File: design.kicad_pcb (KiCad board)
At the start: 2 copper layers, 54.1 x 73.1 mm, 64 parts, among them J2 Programming, J3 HRO_TYPE-C-31-M-12, Q1 Q_PMOS_GSD, SW1 Control, SW2 EN, SW3 IO0, U1 MCP1700-3302E_SOT23, U2 TCK127BG, U3 AP3015, U4 ESP32-C3-WROOM-02-N4, U5 TTP223, U6 TTP223

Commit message: PCB small silkscreen move
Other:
- board text added: "Vbat"
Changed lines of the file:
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@@
     (fp_line (start 9 -3.67) (end 9 -10) (layer "F.SilkS") (width 0.127))
     (fp_line (start 9 -10) (end -9 -10) (layer "F.SilkS") (width 0.127))
-    (fp_circle (center -10.5 -2.9) (end -10.4 -2.9) (layer "F.SilkS") (width 0.2) (fill none))
+    (fp_circle (center -10.22 -2.9) (end -10.12 -2.9) (layer "F.SilkS") (width 0.2) (fill none))
     (fp_line (start 9.75 10.25) (end 9.75 -10.25) (layer "F.CrtYd") (width 0.05))
     (fp_line (start -9.75 10.25) (end 9.75 10.25) (layer "F.CrtYd") (width 0.05))
@@
     (fp_line (start -9 10) (end 9 10) (layer "F.Fab") (width 0.127))
     (fp_line (start 9 10) (end 9 -4) (layer "F.Fab") (width 0.127))
-    (fp_circle (center -10.5 -2.9) (end -10.4 -2.9) (layer "F.Fab") (width 0.2) (fill none))
+    (fp_circle (center -10.22 -2.9) (end -10.12 -2.9) (layer "F.Fab") (width 0.2) (fill none))
     (pad "1" smd rect (at -8.75 -2.9) (size 1.5 0.9) (layers "F.Cu" "F.Paste" "F.Mask")
       (net 2 "+3.3V") (pinfunction "3V3") (pintype "power_in"))
@@
     (effects (font (size 0.5 0.5) (thickness 0.1)))
   )
+  (gr_text "Vbat" (at 166.8 105.5 90) (layer "F.SilkS")
+    (effects (font (size 0.5 0.5) (thickness 0.1)))
+  )

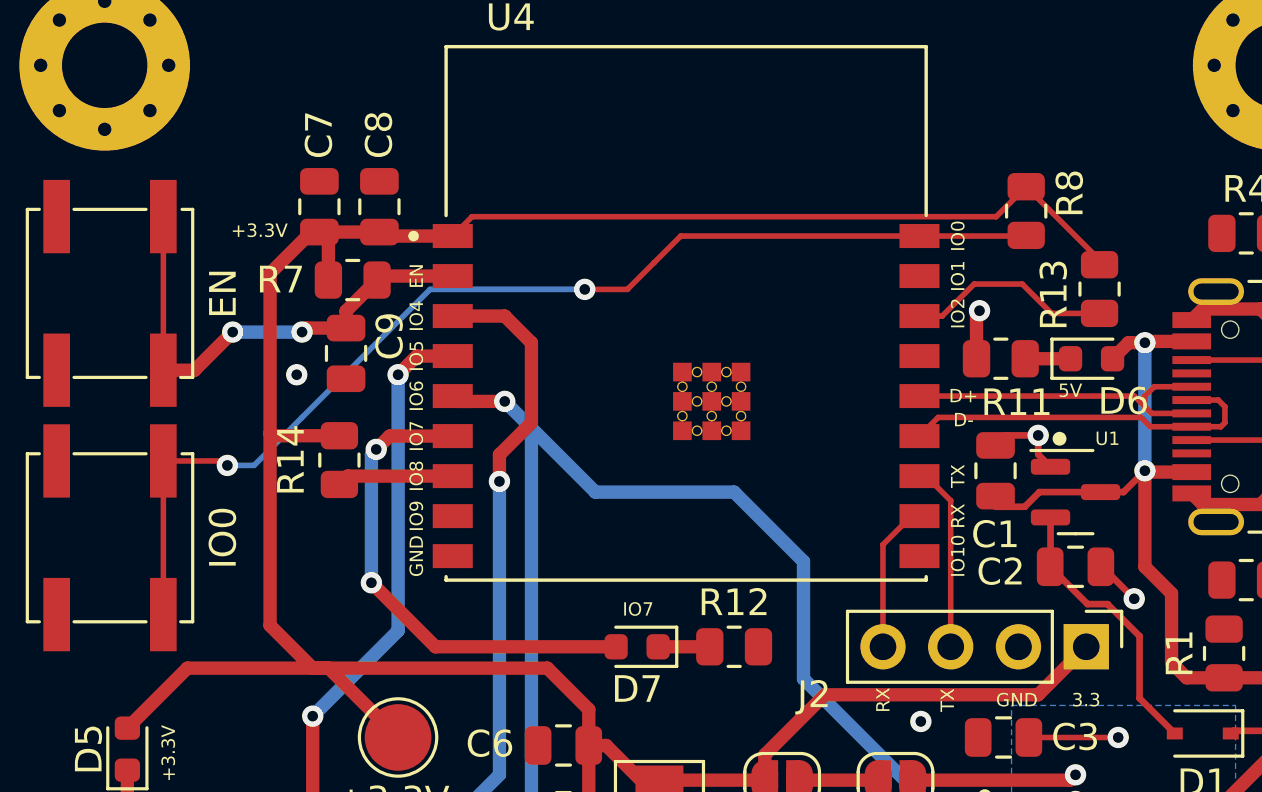
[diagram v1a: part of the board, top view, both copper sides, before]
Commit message: pin IO9 connect to push button instead of IO0 (#11)
* pin IO9 connect to push button instead of IO0
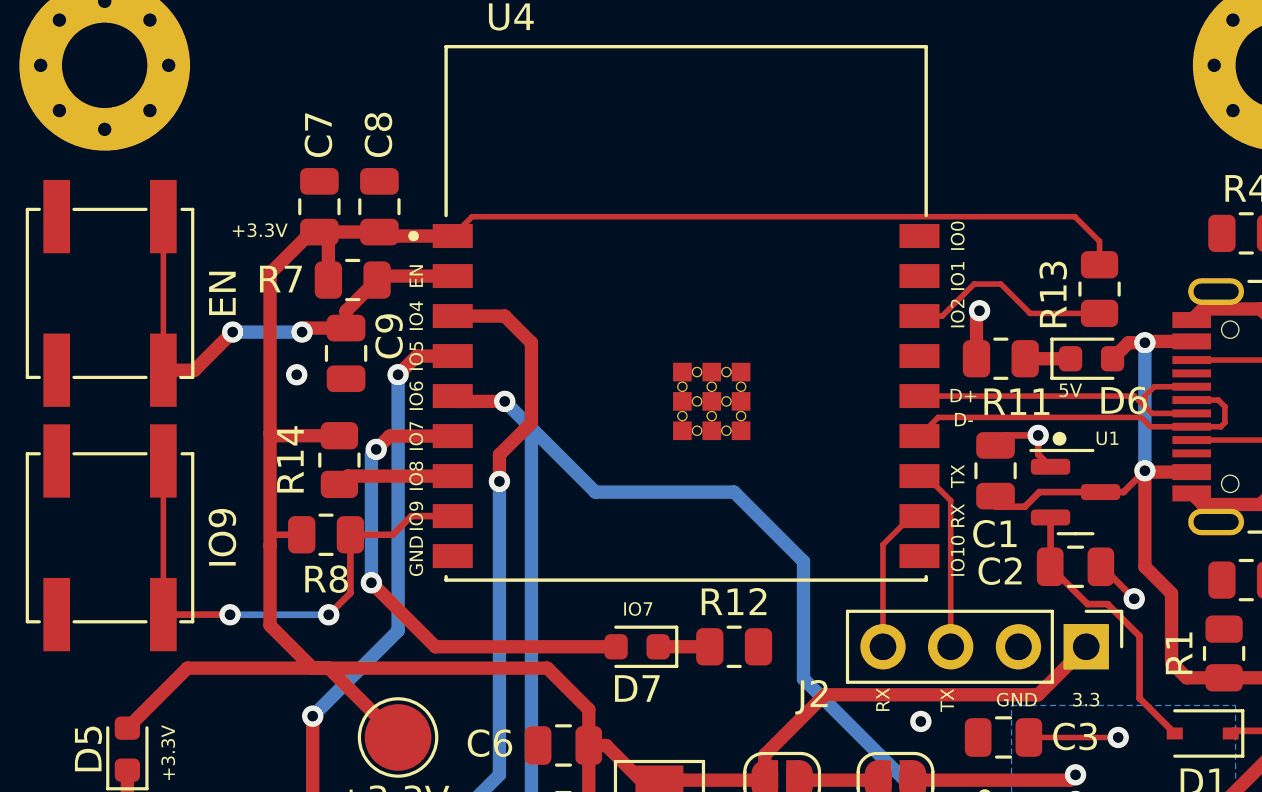
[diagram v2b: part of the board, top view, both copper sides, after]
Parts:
- SW3: value IO0 -> IO9
- moved R8 28.9 mm to (127.5, 87.0), turned to 0 degrees
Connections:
- R8 pad 2: /IO0 -> IO9
- SW3 pad 2: /IO0 -> IO9
- U4 pad 18: /IO0 -> IO0
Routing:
- net /IO0: track 41.8 -> 0.00 mm, vias 2 -> 0
- net IO9: track 0.00 -> 19.4 mm, vias 0 -> 2
- net +3.3V: track 110.7 -> 111.7 mm
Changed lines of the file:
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@@
   (net 32 "/EN")
   (net 33 "/control")
-  (net 34 "/IO0")
+  (net 34 "IO0")
   (net 35 "D+")
   (net 36 "/CC1")
@@
   )
   (footprint "Resistor_SMD:R_0805_2012Metric" (layer "F.Cu")
-    (at 153.75 74.8625 -90)
+    (at 127.5 87)
     (descr "Resistor SMD 0805 (2012 Metric), square (rectangular) end terminal, IPC_7351 nominal, (Body size source: IPC-SM-782 page 72, https://www.pcb-3d.com/wordpress/wp-content/uploads/ipc-sm-782a_amendment_1_and_2.pdf), generated with kicad-footprint-generator")
     (tags "resistor")
@@
     (property "Sheetname" "")
     (attr smd)
-    (fp_text reference "R8" (at -0.6625 -1.65 90) (layer "F.SilkS")
+    (fp_text reference "R8" (at 0 1.7) (layer "F.SilkS")
       (effects (font (size 1 1) (thickness 0.15)))
     )
-    (fp_text value "10K" (at 0 1.65 90) (layer "F.Fab")
+    (fp_text value "10K" (at 0 1.65) (layer "F.Fab")
       (effects (font (size 1 1) (thickness 0.15)))
     )
-    (fp_text user "${REFERENCE}" (at 0 0 90) (layer "F.Fab")
+    (fp_text user "${REFERENCE}" (at 0 0) (layer "F.Fab")
       (effects (font (size 0.5 0.5) (thickness 0.08)))
     )
@@
     (fp_line (start 1 0.625) (end -1 0.625) (layer "F.Fab") (width 0.1))
     (fp_line (start -1 0.625) (end -1 -0.625) (layer "F.Fab") (width 0.1))
-    (pad "1" smd roundrect (at -0.9125 0 270) (size 1.025 1.4) (layers "F.Cu" "F.Paste" "F.Mask") (roundrect_rratio 0.243902)
+    (pad "1" smd roundrect (at -0.9125 0) (size 1.025 1.4) (layers "F.Cu" "F.Paste" "F.Mask") (roundrect_rratio 0.243902)
       (net 2 "+3.3V") (pintype "passive"))
-    (pad "2" smd roundrect (at 0.9125 0 270) (size 1.025 1.4) (layers "F.Cu" "F.Paste" "F.Mask") (roundrect_rratio 0.243902)
-      (net 34 "/IO0") (pintype "passive"))
+    (pad "2" smd roundrect (at 0.9125 0) (size 1.025 1.4) (layers "F.Cu" "F.Paste" "F.Mask") (roundrect_rratio 0.243902)
+      (net 15 "IO9") (pintype "passive"))
     (model "${KICAD6_3DMODEL_DIR}/Resistor_SMD.3dshapes/R_0805_2012Metric.wrl"
       (offset (xyz 0 0 0))
@@
       (effects (font (size 1 1) (thickness 0.15)))
     )
-    (fp_text value "IO0" (at 0 4.25 90) (layer "F.SilkS")
+    (fp_text value "IO9" (at 0 4.25 90) (layer "F.SilkS")
       (effects (font (size 1 1) (thickness 0.15)))
     )
@@
       (net 1 "GND") (pinfunction "1") (pintype "passive"))
     (pad "2" smd rect (at 2.88 2 90) (size 2.75 1) (layers "F.Cu" "F.Paste" "F.Mask")
-      (net 34 "/IO0") (pinfunction "2") (pintype "passive"))
+      (net 15 "IO9") (pinfunction "2") (pintype "passive"))
     (pad "2" smd rect (at -2.88 2 90) (size 2.75 1) (layers "F.Cu" "F.Paste" "F.Mask")
-      (net 34 "/IO0") (pinfunction "2") (pintype "passive"))
+      (net 15 "IO9") (pinfunction "2") (pintype "passive"))
     (model "${KICAD6_3DMODEL_DIR}/Button_Switch_SMD.3dshapes/SW_SPST_EVPBF.wrl"
       (offset (xyz 0 0 0))
@@
       (net 11 "IO1") (pinfunction "IO1") (pintype "bidirectional"))
     (pad "18" smd rect (at 8.75 -2.9) (size 1.5 0.9) (layers "F.Cu" "F.Paste" "F.Mask")
-      (net 34 "/IO0") (pinfunction "IO0") (pintype "bidirectional"))
+      (net 34 "IO0") (pinfunction "IO0") (pintype "bidirectional"))
     (pad "19" smd rect (at -0.14 2.2) (size 0.7 0.7) (layers "F.Cu" "F.Paste" "F.Mask")
       (net 1 "GND") (pinfunction "GND") (pintype "power_in"))
@@
   (segment (start 126.95 75.65) (end 127.25 75.65) (width 0.5) (layer "F.Cu") (net 2))
   (segment (start 129.5 75.65) (end 127.25 75.65) (width 0.5) (layer "F.Cu") (net 2))
-  (segment (start 153.75 73.95) (end 152.625 75.075) (width 0.21) (layer "F.Cu") (net 2))
-  (segment (start 153.75 73.95) (end 156.5 76.7) (width 0.21) (layer "F.Cu") (net 2))
-  (segment (start 132.975 75.075) (end 132.25 75.8) (width 0.21) (layer "F.Cu") (net 2))
+  (segment (start 125.5 87) (end 125.4 87.1) (width 0.25) (layer "F.Cu") (net 2))
+  (segment (start 125.4 87.4) (end 125.4 83.2) (width 0.5) (layer "F.Cu") (net 2))
   (segment (start 129.65 75.8) (end 129.5 75.65) (width 0.5) (layer "F.Cu") (net 2))
-  (segment (start 125.4 90.4) (end 125.4 83.2) (width 0.5) (layer "F.Cu") (net 2))
   (segment (start 135 99.9875) (end 136.0125 99.9875) (width 0.5) (layer "F.Cu") (net 2))
+  (segment (start 125.4 90.4) (end 125.4 87.4) (width 0.5) (layer "F.Cu") (net 2))
   (segment (start 136.0125 99.9875) (end 137.35 98.65) (width 0.5) (layer "F.Cu") (net 2))
   (segment (start 143.95 96.2) (end 140.7 96.2) (width 0.5) (layer "F.Cu") (net 2))
+  (segment (start 126.5875 87) (end 125.5 87) (width 0.25) (layer "F.Cu") (net 2))
   (segment (start 137.35 98.65) (end 137.35 97.4) (width 0.5) (layer "F.Cu") (net 2))
   (segment (start 127.4 92) (end 122.3 92) (width 0.5) (layer "F.Cu") (net 2))
+  (segment (start 155.575 75.075) (end 132.975 75.075) (width 0.21) (layer "F.Cu") (net 2))
   (segment (start 154.2 93) (end 156 91.2) (width 0.5) (layer "F.Cu") (net 2))
+  (segment (start 132.975 75.075) (end 132.25 75.8) (width 0.21) (layer "F.Cu") (net 2))
   (segment (start 137.35 94.9) (end 138 94.9) (width 0.5) (layer "F.Cu") (net 2))
   (segment (start 125.4 83.2) (end 125.4 77.2) (width 0.5) (layer "F.Cu") (net 2))
@@
   (segment (start 127.5875 75.9875) (end 127.25 75.65) (width 0.5) (layer "F.Cu") (net 2))
   (segment (start 137.35 94.9) (end 137.35 93.55) (width 0.5) (layer "F.Cu") (net 2))
-  (segment (start 156.5 76.7) (end 156.5 76.875) (width 0.21) (layer "F.Cu") (net 2))
+  (segment (start 156.5 76) (end 155.575 75.075) (width 0.21) (layer "F.Cu") (net 2))
+  (segment (start 125.4 87.1) (end 125.4 87.4) (width 0.25) (layer "F.Cu") (net 2))
   (segment (start 137.35 97.4) (end 137.35 94.9) (width 0.5) (layer "F.Cu") (net 2))
-  (segment (start 152.625 75.075) (end 132.975 75.075) (width 0.21) (layer "F.Cu") (net 2))
+  (segment (start 156.5 76.875) (end 156.5 76) (width 0.21) (layer "F.Cu") (net 2))
   (segment (start 130.2 94.6) (end 127.6 92) (width 0.5) (layer "F.Cu") (net 2))
   (segment (start 146.2 93) (end 154.2 93) (width 0.5) (layer "F.Cu") (net 2))
@@
   (segment (start 127 93.8) (end 130.2 90.6) (width 0.5) (layer "B.Cu") (net 10))
   (segment (start 130.2 90.6) (end 130.2 81) (width 0.5) (layer "B.Cu") (net 10))
+  (segment (start 153.9 78.7) (end 152.8 77.6) (width 0.21) (layer "F.Cu") (net 12))
   (segment (start 151.8 77.6) (end 150.6 78.8) (width 0.21) (layer "F.Cu") (net 12))
-  (segment (start 153.6 77.6) (end 151.8 77.6) (width 0.21) (layer "F.Cu") (net 12))
-  (segment (start 154.7 78.7) (end 153.6 77.6) (width 0.21) (layer "F.Cu") (net 12))
+  (segment (start 152.8 77.6) (end 151.8 77.6) (width 0.21) (layer "F.Cu") (net 12))
+  (segment (start 156.5 78.7) (end 153.9 78.7) (width 0.21) (layer "F.Cu") (net 12))
   (segment (start 150.6 78.8) (end 149.75 78.8) (width 0.21) (layer "F.Cu") (net 12))
-  (segment (start 156.5 78.7) (end 154.7 78.7) (width 0.21) (layer "F.Cu") (net 12))
   (segment (start 128.3125 84.8) (end 128 85.1125) (width 0.5) (layer "F.Cu") (net 14))
   (segment (start 132.25 84.8) (end 128.3125 84.8) (width 0.5) (layer "F.Cu") (net 14))
+  (segment (start 128.4125 89.1875) (end 128.4125 87) (width 0.25) (layer "F.Cu") (net 15))
+  (segment (start 132.25 86.3) (end 130.7 86.3) (width 0.25) (layer "F.Cu") (net 15))
+  (segment (start 130 87) (end 128.4125 87) (width 0.25) (layer "F.Cu") (net 15))
+  (segment (start 130.7 86.3) (end 130 87) (width 0.25) (layer "F.Cu") (net 15))
+  (segment (start 123.9 90) (end 123.8925 89.9925) (width 0.25) (layer "F.Cu") (net 15))
+  (segment (start 127.6 90) (end 128.4125 89.1875) (width 0.25) (layer "F.Cu") (net 15))
+  (segment (start 123.8925 89.9925) (end 121.4 89.9925) (width 0.25) (layer "F.Cu") (net 15))
+  (segment (start 121.4 84.2325) (end 121.4 89.9925) (width 0.21) (layer "F.Cu") (net 15))
+  (via (at 127.6 90) (size 0.8) (drill 0.4) (layers "F.Cu" "B.Cu") (net 15))
+  (via (at 123.9 90) (size 0.8) (drill 0.4) (layers "F.Cu" "B.Cu") (net 15))
+  (segment (start 127.6 90) (end 123.9 90) (width 0.25) (layer "B.Cu") (net 15))
   (segment (start 166.2 93.8625) (end 165.7375 93.4) (width 0.25) (layer "F.Cu") (net 17))
   (segment (start 166.2 104.2125) (end 165.6 104.8125) (width 0.25) (layer "F.Cu") (net 17))
@@
   (segment (start 154.85 103.27) (end 153.92 104.2) (width 0.5) (layer "F.Cu") (net 33))
   (segment (start 153.92 104.2) (end 159.68 104.2) (width 0.5) (layer "F.Cu") (net 33))
-  (segment (start 139.8 76.8) (end 138.8 77.8) (width 0.21) (layer "F.Cu") (net 34))
-  (segment (start 123.8 84.4) (end 123.6325 84.2325) (width 0.21) (layer "F.Cu") (net 34))
-  (segment (start 153.725 75.8) (end 149.75 75.8) (width 0.21) (layer "F.Cu") (net 34))
-  (segment (start 140.8 75.8) (end 139.8 76.8) (width 0.21) (layer "F.Cu") (net 34))
-  (segment (start 153.75 75.775) (end 153.725 75.8) (width 0.21) (layer "F.Cu") (net 34))
-  (segment (start 123.6325 84.2325) (end 121.4 84.2325) (width 0.21) (layer "F.Cu") (net 34))
-  (segment (start 138.8 77.8) (end 137.2 77.8) (width 0.21) (layer "F.Cu") (net 34))
-  (segment (start 149.75 75.8) (end 140.8 75.8) (width 0.21) (layer "F.Cu") (net 34))
-  (segment (start 121.4 84.2325) (end 121.4 89.9925) (width 0.21) (layer "F.Cu") (net 34))
-  (via (at 123.8 84.4) (size 0.8) (drill 0.4) (layers "F.Cu" "B.Cu") (net 34))
-  (via (at 137.2 77.8) (size 0.8) (drill 0.4) (layers "F.Cu" "B.Cu") (net 34))
-  (segment (start 126.6 82.6) (end 124.8 84.4) (width 0.21) (layer "B.Cu") (net 34))
-  (segment (start 131.4 77.8) (end 126.6 82.6) (width 0.21) (layer "B.Cu") (net 34))
-  (segment (start 124.8 84.4) (end 123.8 84.4) (width 0.21) (layer "B.Cu") (net 34))
-  (segment (start 137.2 77.8) (end 131.4 77.8) (width 0.21) (layer "B.Cu") (net 34))
   (segment (start 157.8 81.8) (end 158.2 82.2) (width 0.21) (layer "F.Cu") (net 35))
   (segment (start 149.75 81.8) (end 157.8 81.8) (width 0.21) (layer "F.Cu") (net 35))
